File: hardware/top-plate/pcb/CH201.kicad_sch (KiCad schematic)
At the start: 30 parts

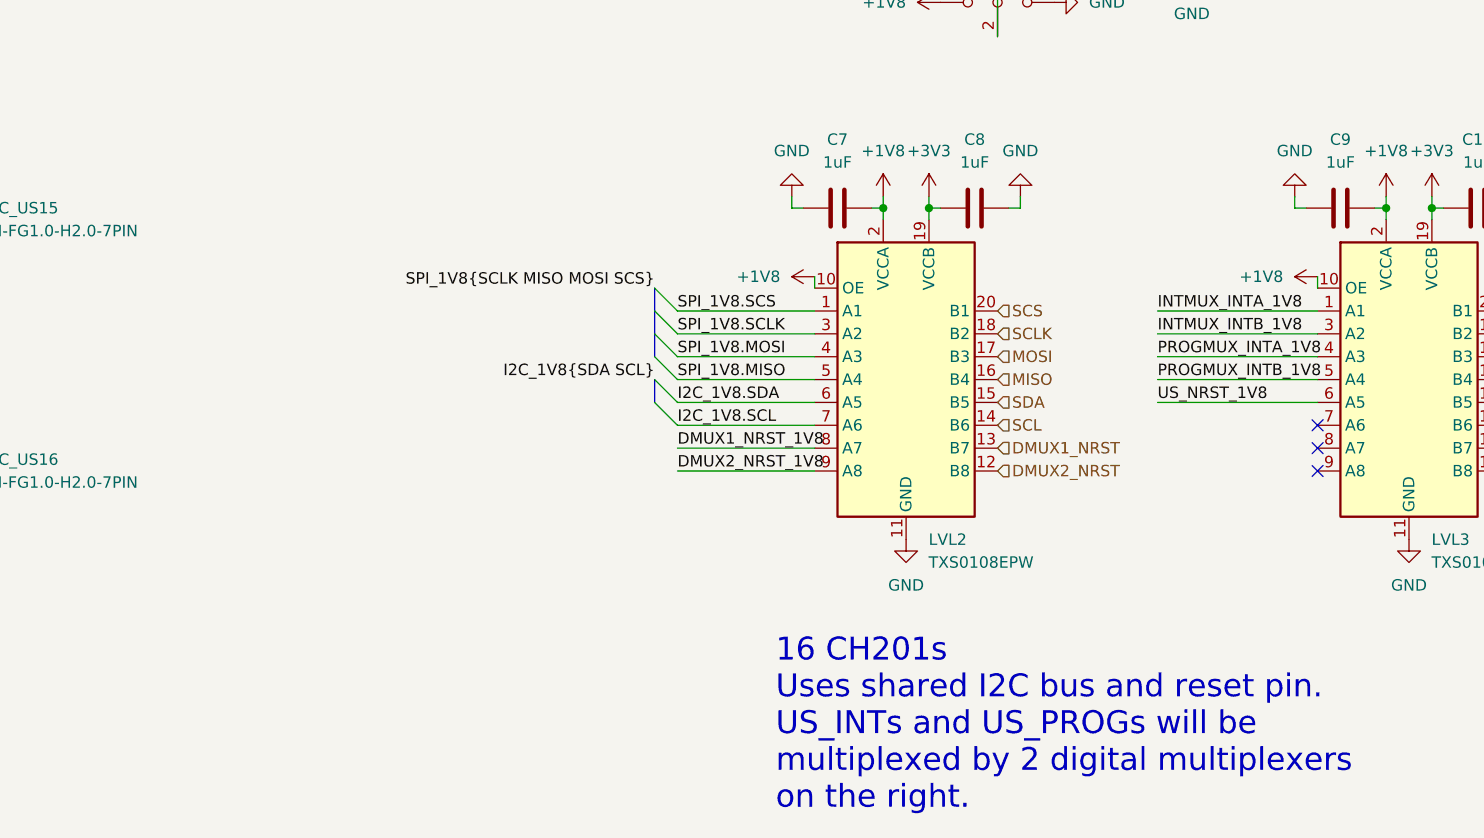
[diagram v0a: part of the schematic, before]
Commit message: fixed up symbols and footprints for top plate, and completed top plate schematic (other than modifications for better routing)
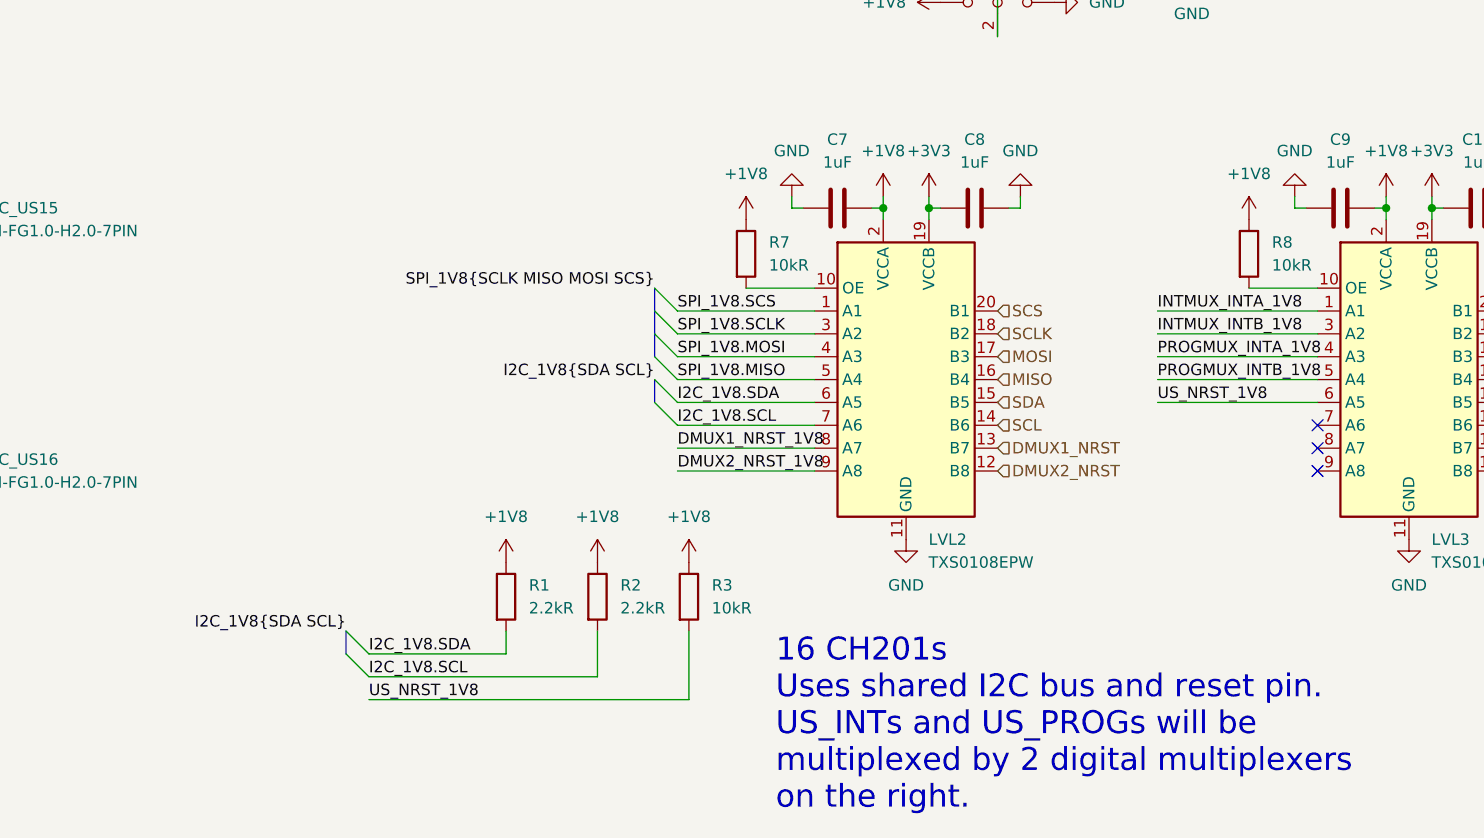
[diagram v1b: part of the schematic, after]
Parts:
- added R1, R2: 2.2kR, PCM_Resistor_SMD_AKL:R_1206_3216Metric_Pad1.30x1.75mm_HandSolder, symbol Device:R
- added R3, R7, R8: 10kR, PCM_Resistor_SMD_AKL:R_1206_3216Metric_Pad1.30x1.75mm_HandSolder, symbol Device:R
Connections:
- net +1V8: now also R1.1, R2.1, R3.1, R7.1, R8.1; no longer LVL2.10 (OE), LVL3.10 (OE)
- net I2C_1V8.SCL: now also R2.2
- net I2C_1V8.SDA: now also R1.2
- net US_NRST_1V8: now also R3.2
- new net: LVL3.10 (OE), R8.2
- new net: LVL2.10 (OE), R7.2
